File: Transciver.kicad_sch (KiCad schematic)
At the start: 5 parts, among them SW1 SW_DIP_x02

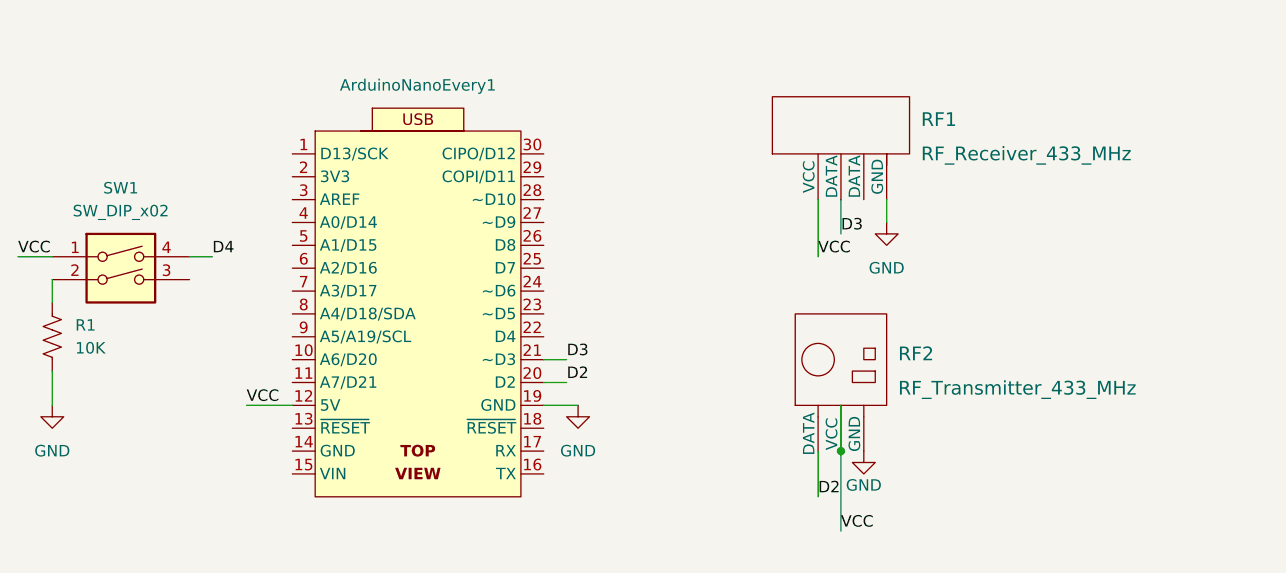
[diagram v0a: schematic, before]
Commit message: VCC, GND and D4 annotate correctly
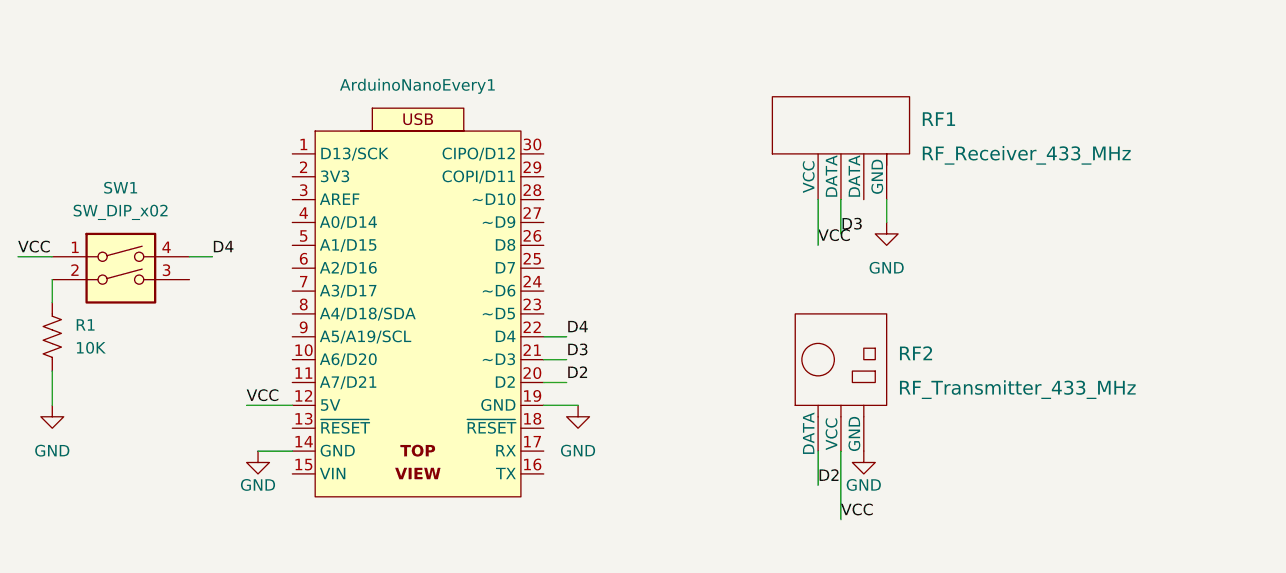
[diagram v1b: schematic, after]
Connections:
- net D4: now also ArduinoNanoEvery1.22 (D4)
- net GND: now also ArduinoNanoEvery1.14 (GND)
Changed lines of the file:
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@@
 (kicad_sch (version 20211123) (generator eeschema)
   (paper "A4")
-  (junction (at 114.3 69.85) (diameter 0) (color 0 0 0 0)
-  )
-  (wire (pts (xy 114.3 78.74) (xy 114.3 69.85))
+  (wire (pts (xy 114.3 77.47) (xy 114.3 69.85))
     (stroke (width 0) (type default) (color 0 0 0 0))
   )
@@
     (stroke (width 0) (type default) (color 0 0 0 0))
   )
+  (wire (pts (xy 49.53 69.85) (xy 53.34 69.85))
+    (stroke (width 0) (type default) (color 0 0 0 0))
+  )
   (wire (pts (xy 44.45 48.26) (xy 41.91 48.26))
     (stroke (width 0) (type default) (color 0 0 0 0))
   )
-  (wire (pts (xy 111.76 48.26) (xy 111.76 41.91))
+  (wire (pts (xy 111.76 46.99) (xy 111.76 41.91))
+    (stroke (width 0) (type default) (color 0 0 0 0))
+  )
+  (wire (pts (xy 83.82 57.15) (xy 81.28 57.15))
     (stroke (width 0) (type default) (color 0 0 0 0))
   )
@@
     (stroke (width 0) (type default) (color 0 0 0 0))
   )
-  (wire (pts (xy 111.76 74.93) (xy 111.76 69.85))
-    (stroke (width 0) (type default) (color 0 0 0 0))
-  )
-  (wire (pts (xy 114.3 64.77) (xy 114.3 69.85))
+  (wire (pts (xy 111.76 73.66) (xy 111.76 69.85))
     (stroke (width 0) (type default) (color 0 0 0 0))
   )
@@
     (stroke (width 0) (type default) (color 0 0 0 0))
   )
-  (label "VCC" (at 114.3 78.74 0)
-    (effects (font (size 1.27 1.27)) (justify left bottom))
-  )
-  (label "VCC" (at 111.76 48.26 0)
+  (label "VCC" (at 114.3 77.47 0)
+    (effects (font (size 1.27 1.27)) (justify left bottom))
+  )
+  (label "VCC" (at 111.76 46.99 0)
     (effects (font (size 1.27 1.27)) (justify left bottom))
   )
@@
     (effects (font (size 1.27 1.27)) (justify left bottom))
   )
+  (label "D4" (at 83.82 57.15 0)
+    (effects (font (size 1.27 1.27)) (justify left bottom))
+  )
   (label "D3" (at 114.3 45.72 0)
     (effects (font (size 1.27 1.27)) (justify left bottom))
   )
-  (label "D2" (at 111.76 74.93 0)
+  (label "D2" (at 111.76 73.66 0)
     (effects (font (size 1.27 1.27)) (justify left bottom))
   )
@@
     (pin "3")
     (pin "4")
+  )
+  (symbol (lib_id "power:GND") (at 49.53 69.85 0) (unit 1)
+    (in_bom yes) (on_board yes)
+    (property "Reference" "#PWR?" (id 0) (at 49.53 76.2 0)
+      (effects (font (size 1.27 1.27)) hide)
+    )
+    (property "Value" "GND" (id 1) (at 49.53 73.66 0))
+    (property "Footprint" "" (id 2) (at 49.53 69.85 0)
+      (effects (font (size 1.27 1.27)) hide)
+    )
+    (property "Datasheet" "" (id 3) (at 49.53 69.85 0)
+      (effects (font (size 1.27 1.27)) hide)
+    )
+    (pin "1")
   )
   (symbol (lib_id "sensors:RF_Receiver_433_MHz") (at 114.3 41.91 0) (unit 1)
@@
       (reference "#PWR04") (unit 1) (value "GND") (footprint "")
     )
+    (path "/48c0f4e0-ab62-4181-b70e-105b653a1425"
+      (reference "#PWR?") (unit 1) (value "GND") (footprint "")
+    )
     (path "/bd966995-2adb-4b59-8ae1-4522d2a4b5db"

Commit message: Debug Led and Resistor added
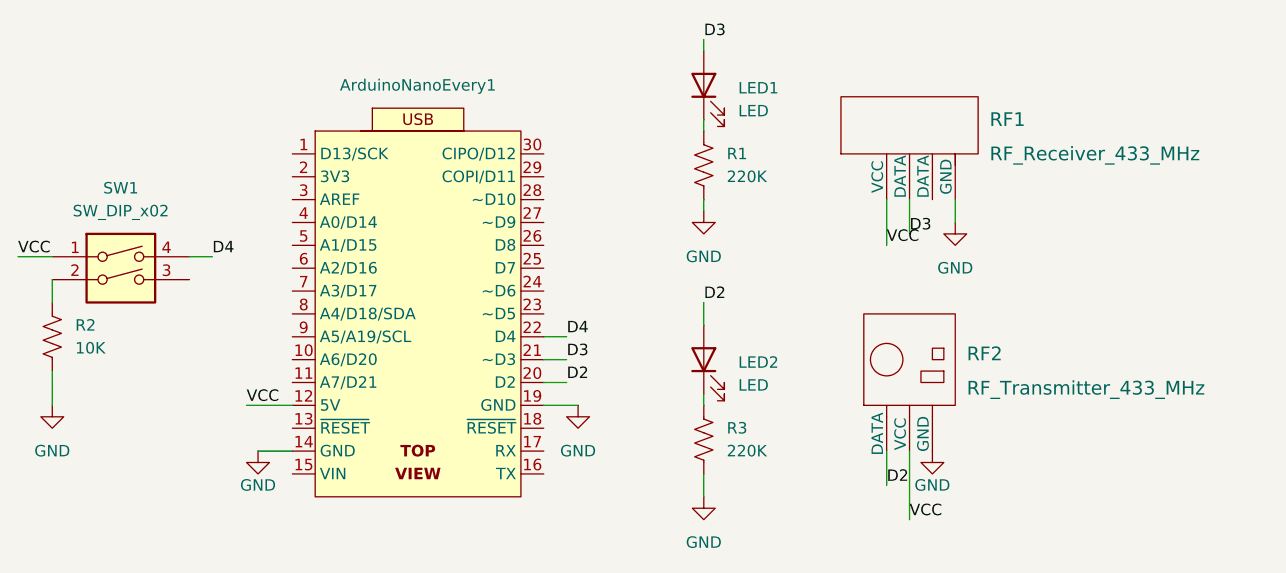
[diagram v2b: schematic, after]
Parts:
- added LED1, LED2: LED, LED_THT:LED_D3.0mm, symbol Device:LED
- added R1, R3: 220K, Resistor_THT:R_Axial_DIN0309_L9.0mm_D3.2mm_P15.24mm_Horizontal, symbol Device:R_US
- R2: renamed from R1; footprint (none) -> Resistor_THT:R_Axial_DIN0309_L9.0mm_D3.2mm_P15.24mm_Horizontal
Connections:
- net D2: now also LED2.2 (A)
- net D3: now also LED1.2 (A)
- net GND: now also R1.2, R3.2
- new net: LED2.1 (K), R3.1
- new net: LED1.1 (K), R1.1
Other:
- title: (none) -> 433_Nano_Transciver
- moved on the sheet: RF1, RF2
